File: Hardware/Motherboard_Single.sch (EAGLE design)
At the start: 63 parts, among them J1 MICROMOD-2222-C, J10 MICRO-SD-PUSH-PUSH-EXT-PIN, J2 Vertical Qwiic Connector, J4 QWIIC_RIGHT_ANGLE, J5 CORTEX_JTAG_DEBUG_MINIMUM_PTH, J6 MICROMOD_CARRIER, U2 MCP73831, U5 AP7361C-33

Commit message: Adds another standoff for qwiic boards around the lower left edge, adds silk
* Removes jumper for "VIN/VUSB"
* Correctly routes USB_VIN on processor connector to VIN
* Double routes PWR_EN for ESP32 Processor boards
* Moves SD Card up 0.04"
* Adds more measures
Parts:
- removed JP1: JUMPER-SMT_2_NC_TRACE_SILK, SparkFun-Jumpers:JUMPER-SMT_2_NC_TRACE_SILK
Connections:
- removed net USB_VIN: J1.USB_VIN
- removed net V_USB: BYP.2, F2.2, JP1.1, TP4.1
- net PWR_EN0: now also J1.AUD_LRCLK
- net VIN: now also BYP.2, F2.2, J1.USB_VIN, TP4.1; no longer JP1.2
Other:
- note added: "Buttons"
- note added: "v10"
- note removed: "Buttons and Switch"
- note removed: "v01"
- moved on the sheet: J13, S1, S2

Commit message: Adds 2 pin dip switch for charge selection, adds PCHAN MOSFET to VBATT net
* Adds better silk
* Moves stuff around schematic for better clarity
* Adds charge table to schematic
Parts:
- removed D7: 3A/10V/280mV, SparkFun-DiscreteSemi:DIODE-SCHOTTKY-BAT60A
- removed R6: 2.0k, SparkFun-Resistors:2.0KOHM-0603-1/10W-5%
- added Q1: 20V/4.2A/52mΩ/1.4W, SparkFun-DiscreteSemi:MOSFET_PCH-DMG2305UX-7
- added R3: 2.0k, SparkFun-Resistors:2.0KOHM-0603-1/10W-5%
- added R4: 10k, SparkFun-Resistors:10KOHM-0603-1/10W-1%
- added S3: DIP-02-SMD-50MIL, SparkFun-Switches:DIP-02-SMD-50MIL
- LOGO3: value OSHW-LOGOMINI -> OSHW-LOGOL; device SparkFun-Aesthetics:OSHW-LOGOMINI -> SparkFun-Aesthetics:OSHW-LOGOL
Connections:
- new net N$11: R4.2, S3.P$2
- new net N$7: R3.2, S3.P$1
- net GND: now also R3.1, R4.1; no longer R6.1
- net N$8: now also S3.P$3, S3.P$4; no longer R6.2
- net VCC: now also Q1.S; no longer D7.C
- net VIN: now also Q1.G
- net V_BATT: now also Q1.D; no longer D7.A
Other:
- note added: "1"
- note added: "1+2"
- note added: "100mA"
- note added: "166mA"
- note added: "2"
- note added: "500mA"
- note added: "Charge Current Selection"
- note added: "Standoff"
- note added: "Standoffs"
- note removed: "Charge current: 500mA (1000V/Rprog)"
- moved on the sheet: C3, C4, D4, D5, J13, J2, J4, J8, R5, S1, S2, TP1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

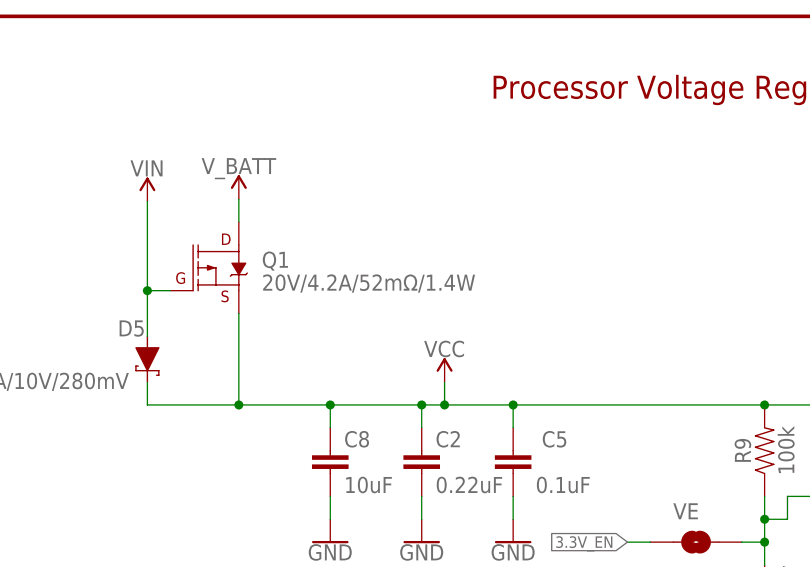
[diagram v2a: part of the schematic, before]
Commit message: Replaces MOSFET with another one
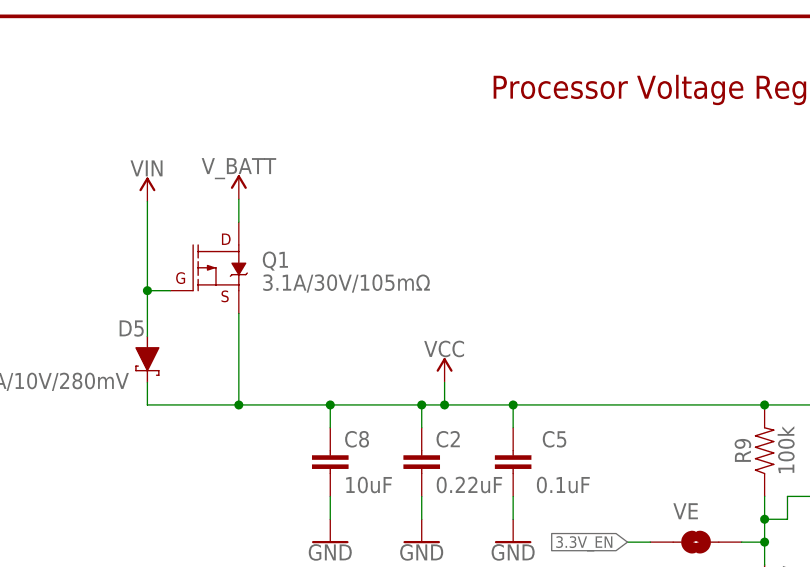
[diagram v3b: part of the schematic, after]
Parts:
- Q1: value 20V/4.2A/52mΩ/1.4W -> 3.1A/30V/105mΩ; device SparkFun-DiscreteSemi:MOSFET_PCH-DMG2305UX-7 -> SparkFun-DiscreteSemi:MOSFET_PCH-DMG2307L
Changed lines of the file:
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@@
 <part name="R4" library="SparkFun-Resistors" deviceset="10KOHM" device="-0603-1/10W-1%" value="10k"/>
 <part name="GND3" library="SparkFun-PowerSymbols" deviceset="GND" device=""/>
-<part name="Q1" library="SparkFun-DiscreteSemi" deviceset="MOSFET_PCH" device="-DMG2305UX-7" value="20V/4.2A/52mΩ/1.4W"/>
+<part name="Q1" library="SparkFun-DiscreteSemi" deviceset="MOSFET_PCH" device="-DMG2307L" value="3.1A/30V/105mΩ"/>
 <part name="GND5" library="SparkFun-PowerSymbols" deviceset="GND" device=""/>
 </parts>

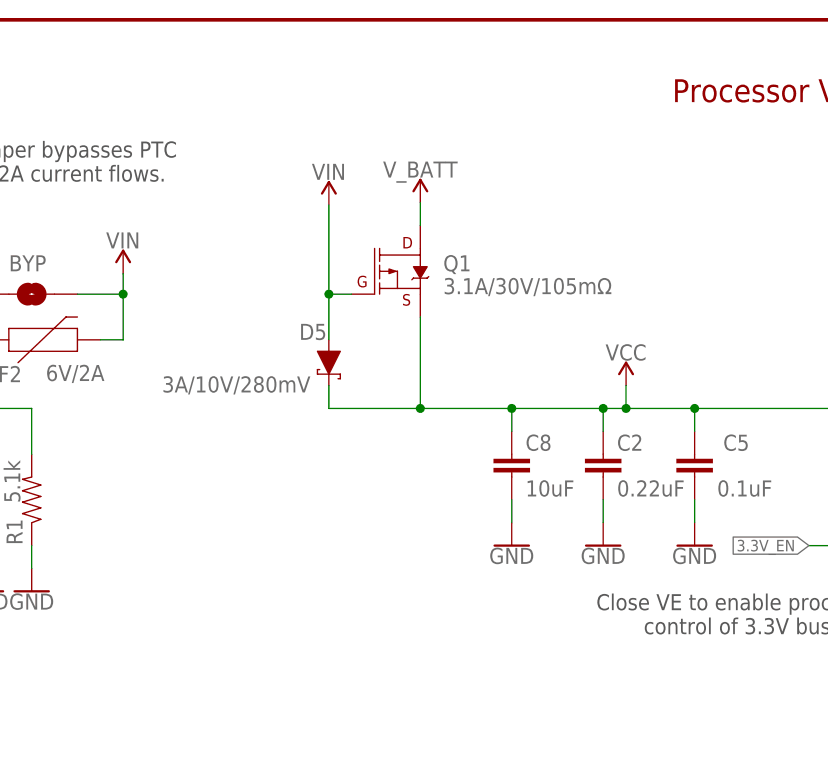
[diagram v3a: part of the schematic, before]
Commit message: Adds 10k pulldown to gate on PCHAN MOSFET, fixes length measurement
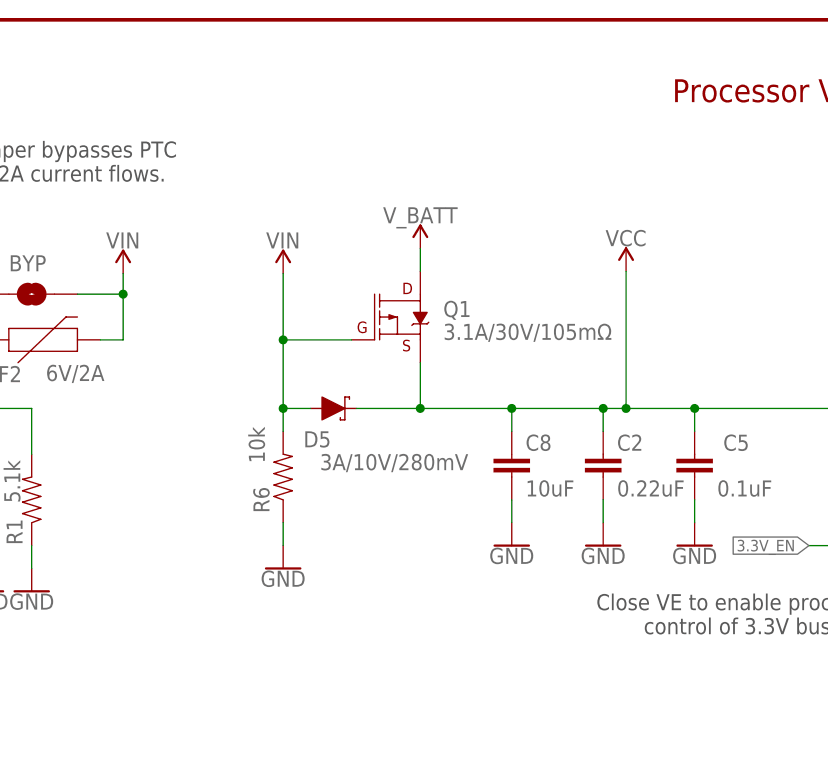
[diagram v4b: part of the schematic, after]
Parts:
- added R6: 10k, SparkFun-Resistors:10KOHM-0603-1/10W-1%
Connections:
- net GND: now also R6.1
- net VIN: now also R6.2
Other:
- moved on the sheet: D5, Q1
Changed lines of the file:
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@@
 <part name="Q1" library="SparkFun-DiscreteSemi" deviceset="MOSFET_PCH" device="-DMG2307L" value="3.1A/30V/105mΩ"/>
 <part name="GND5" library="SparkFun-PowerSymbols" deviceset="GND" device=""/>
+<part name="R6" library="SparkFun-Resistors" deviceset="10KOHM" device="-0603-1/10W-1%" value="10k"/>
+<part name="GND6" library="SparkFun-PowerSymbols" deviceset="GND" device=""/>
 </parts>
 <sheets>
@@
 <attribute name="VALUE" x="238.76" y="215.646" size="1.778" layer="96" rot="MR0" align="top-center"/>
 </instance>
-<instance part="SUPPLY27" gate="G$1" x="281.94" y="259.08" smashed="yes">
-<attribute name="VALUE" x="281.94" y="261.874" size="1.778" layer="96" align="bottom-center"/>
+<instance part="SUPPLY27" gate="G$1" x="281.94" y="254" smashed="yes">
+<attribute name="VALUE" x="281.94" y="256.794" size="1.778" layer="96" align="bottom-center"/>
 </instance>
 <instance part="U5" gate="G$1" x="360.68" y="231.14" smashed="yes">
@@
 <attribute name="VALUE" x="293.624" y="226.441" size="1.778" layer="96" font="vector"/>
 </instance>
-<instance part="SUPPLY28" gate="G$1" x="304.8" y="238.76" smashed="yes">
-<attribute name="VALUE" x="304.8" y="241.554" size="1.778" layer="96" align="bottom-center"/>
-</instance>
-<instance part="D5" gate="G$1" x="271.78" y="241.3" smashed="yes" rot="R270">
-<attribute name="NAME" x="268.478" y="243.84" size="1.778" layer="95" font="vector"/>
-<attribute name="VALUE" x="253.238" y="239.776" size="1.778" layer="96" font="vector" align="top-left"/>
+<instance part="SUPPLY28" gate="G$1" x="304.8" y="251.46" smashed="yes">
+<attribute name="VALUE" x="304.8" y="254.254" size="1.778" layer="96" align="bottom-center"/>
+</instance>
+<instance part="D5" gate="G$1" x="272.288" y="236.22" smashed="yes">
+<attribute name="NAME" x="272.034" y="233.68" size="1.778" layer="95" font="vector" rot="R180"/>
+<attribute name="VALUE" x="287.274" y="229.362" size="1.778" layer="96" font="vector" rot="R180" align="top-left"/>
 </instance>
 <instance part="5V_LED" gate="G$1" x="378.714" y="61.722" smashed="yes" rot="R90">
@@
 <attribute name="VALUE" x="378.714" y="51.308" size="1.778" layer="96" align="top-center"/>
 </instance>
-<instance part="SUPPLY13" gate="G$1" x="271.78" y="258.826" smashed="yes">
-<attribute name="VALUE" x="271.78" y="261.62" size="1.778" layer="96" align="bottom-center"/>
+<instance part="SUPPLY13" gate="G$1" x="266.7" y="251.206" smashed="yes">
+<attribute name="VALUE" x="266.7" y="254" size="1.778" layer="96" align="bottom-center"/>
 </instance>
 <instance part="SUPPLY24" gate="G$1" x="378.714" y="92.456" smashed="yes">
@@
 <attribute name="VALUE" x="276.86" y="131.826" size="1.778" layer="96" font="vector" rot="MR0" align="top-center"/>
 </instance>
-<instance part="Q1" gate="G$1" x="279.4" y="251.46" smashed="yes">
-<attribute name="NAME" x="284.48" y="251.46" size="1.778" layer="95" font="vector"/>
-<attribute name="VALUE" x="284.48" y="248.92" size="1.778" layer="96" font="vector"/>
+<instance part="Q1" gate="G$1" x="279.4" y="246.38" smashed="yes">
+<attribute name="NAME" x="284.48" y="246.38" size="1.778" layer="95" font="vector"/>
+<attribute name="VALUE" x="284.48" y="243.84" size="1.778" layer="96" font="vector"/>
 </instance>
 <instance part="GND5" gate="1" x="193.04" y="5.08" smashed="yes">
 <attribute name="VALUE" x="193.04" y="4.826" size="1.778" layer="96" font="vector" align="top-center"/>
+</instance>
+<instance part="R6" gate="G$1" x="266.7" y="228.6" smashed="yes" rot="R90">
+<attribute name="NAME" x="265.176" y="226.06" size="1.778" layer="95" font="vector" rot="R90" align="bottom-center"/>
+<attribute name="VALUE" x="262.89" y="232.156" size="1.778" layer="96" font="vector" rot="R90" align="top-center"/>
+</instance>
+<instance part="GND6" gate="1" x="266.7" y="218.44" smashed="yes">
+<attribute name="VALUE" x="266.7" y="218.186" size="1.778" layer="96" align="top-center"/>
 </instance>
 </instances>
@@
 <wire x1="192.024" y1="164.338" x2="192.024" y2="166.878" width="0.1524" layer="91"/>
 </segment>
+<segment>
+<pinref part="R6" gate="G$1" pin="1"/>
+<wire x1="266.7" y1="223.52" x2="266.7" y2="220.98" width="0.1524" layer="91"/>
+<pinref part="GND6" gate="1" pin="GND"/>
+</segment>
 </net>
 <net name="PWR_EN0" class="0">
@@
 <pinref part="D5" gate="G$1" pin="A"/>
 <pinref part="SUPPLY13" gate="G$1" pin="VIN"/>
-<wire x1="271.78" y1="243.84" x2="271.78" y2="248.92" width="0.1524" layer="91"/>
 <pinref part="Q1" gate="G$1" pin="G"/>
-<wire x1="271.78" y1="248.92" x2="271.78" y2="258.826" width="0.1524" layer="91"/>
-<wire x1="274.32" y1="248.92" x2="271.78" y2="248.92" width="0.1524" layer="91"/>
-<junction x="271.78" y="248.92"/>
+<wire x1="274.32" y1="243.84" x2="266.7" y2="243.84" width="0.1524" layer="91"/>
+<wire x1="266.7" y1="243.84" x2="266.7" y2="251.206" width="0.1524" layer="91"/>
+<pinref part="R6" gate="G$1" pin="2"/>
+<wire x1="266.7" y1="233.68" x2="266.7" y2="236.22" width="0.1524" layer="91"/>
+<junction x="266.7" y="243.84"/>
+<wire x1="266.7" y1="236.22" x2="266.7" y2="243.84" width="0.1524" layer="91"/>
+<wire x1="269.748" y1="236.22" x2="266.7" y2="236.22" width="0.1524" layer="91"/>
+<junction x="266.7" y="236.22"/>
 </segment>
 <segment>
@@
 <pinref part="Q1" gate="G$1" pin="D"/>
 <pinref part="SUPPLY27" gate="G$1" pin="V_BATT"/>
-<wire x1="281.94" y1="259.08" x2="281.94" y2="256.54" width="0.1524" layer="91"/>
+<wire x1="281.94" y1="254" x2="281.94" y2="251.46" width="0.1524" layer="91"/>
 </segment>
 </net>
@@
 <pinref part="C8" gate="G$1" pin="1"/>
 <pinref part="SUPPLY28" gate="G$1" pin="VCC"/>
-<wire x1="304.8" y1="236.22" x2="304.8" y2="238.76" width="0.1524" layer="91"/>
+<wire x1="304.8" y1="236.22" x2="304.8" y2="251.46" width="0.1524" layer="91"/>
 <junction x="304.8" y="236.22"/>
 <wire x1="292.1" y1="236.22" x2="281.94" y2="236.22" width="0.1524" layer="91"/>
 <junction x="292.1" y="236.22"/>
 <pinref part="D5" gate="G$1" pin="C"/>
-<wire x1="281.94" y1="236.22" x2="271.78" y2="236.22" width="0.1524" layer="91"/>
-<wire x1="271.78" y1="236.22" x2="271.78" y2="238.76" width="0.1524" layer="91"/>
+<wire x1="281.94" y1="236.22" x2="274.828" y2="236.22" width="0.1524" layer="91"/>
 <pinref part="Q1" gate="G$1" pin="S"/>
-<wire x1="281.94" y1="246.38" x2="281.94" y2="236.22" width="0.1524" layer="91"/>
+<wire x1="281.94" y1="241.3" x2="281.94" y2="236.22" width="0.1524" layer="91"/>
 <junction x="281.94" y="236.22"/>
 </segment>

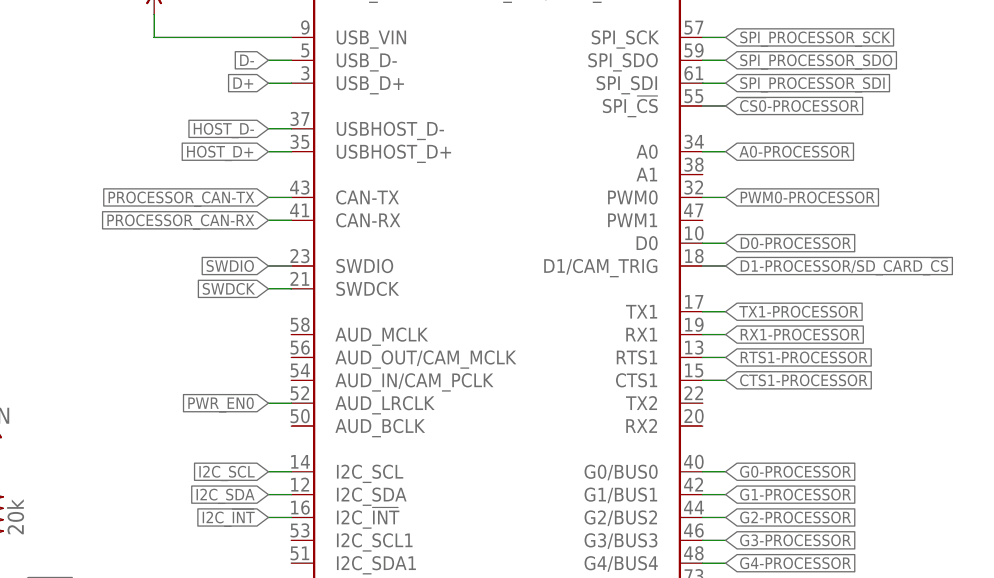
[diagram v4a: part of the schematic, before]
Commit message: Adds prod_id to function board connector, double routes power enable to A1 and previous pin
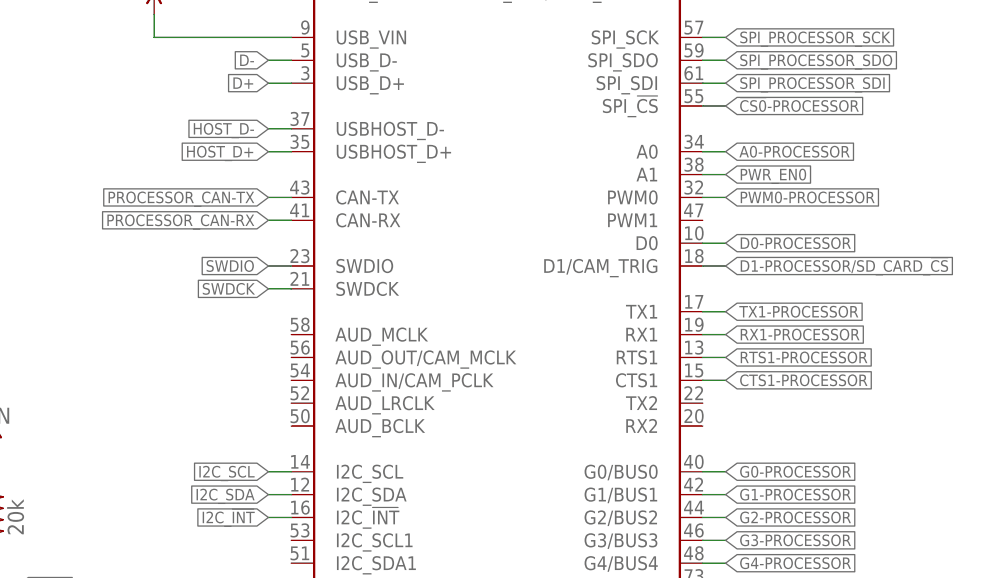
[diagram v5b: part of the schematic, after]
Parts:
- H3, H4, H8: value STAND-OFF-REFLOW2.5MM_TALL -> STAND-OFF-REFLOW-M2.5_2.5MM_TALL; device SparkFun-Hardware:STAND-OFF-REFLOW2.5MM_TALL -> SparkFun-Hardware:STAND-OFF-REFLOW-M2.5_2.5MM_TALL
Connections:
- net PWR_EN0: now also J1.A1; no longer J1.AUD_LRCLK
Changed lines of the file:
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@@
 <part name="J4" library="SparkFun-Connectors" deviceset="QWIIC_CONNECTOR" device="JS-1MM" value="QWIIC_RIGHT_ANGLE"/>
 <part name="FRAME1" library="SparkFun-Aesthetics" deviceset="FRAME-LEDGER" device=""/>
-<part name="H3" library="SparkFun-Hardware" deviceset="STAND-OFF-REFLOW" device="2.5MM_TALL"/>
-<part name="H8" library="SparkFun-Hardware" deviceset="STAND-OFF-REFLOW" device="2.5MM_TALL"/>
+<part name="H3" library="SparkFun-Hardware" deviceset="STAND-OFF-REFLOW" device="-M2.5_2.5MM_TALL"/>
+<part name="H8" library="SparkFun-Hardware" deviceset="STAND-OFF-REFLOW" device="-M2.5_2.5MM_TALL"/>
 <part name="H14" library="SparkFun-Hardware" deviceset="STAND-OFF" device="TIGHT"/>
 <part name="H15" library="SparkFun-Hardware" deviceset="STAND-OFF" device="TIGHT"/>
@@
 <part name="C12" library="SparkFun-Capacitors" deviceset="0.1UF" device="-0603-25V-(+80/-20%)" value="0.1uF"/>
 <part name="GND36" library="SparkFun-PowerSymbols" deviceset="GND" device=""/>
-<part name="H4" library="SparkFun-Hardware" deviceset="STAND-OFF-REFLOW" device="2.5MM_TALL"/>
+<part name="H4" library="SparkFun-Hardware" deviceset="STAND-OFF-REFLOW" device="-M2.5_2.5MM_TALL"/>
 <part name="GND40" library="SparkFun-PowerSymbols" deviceset="GND" device=""/>
 <part name="SUPPLY9" library="SparkFun-PowerSymbols" deviceset="VIN" device=""/>
@@
 </segment>
 <segment>
-<wire x1="73.66" y1="66.04" x2="71.12" y2="66.04" width="0.1524" layer="91"/>
-<label x="71.12" y="66.04" size="1.27" layer="95" font="vector" rot="R180" xref="yes"/>
-<pinref part="J1" gate="J1" pin="AUD_LRCLK"/>
+<pinref part="J1" gate="J1" pin="A1"/>
+<wire x1="121.92" y1="91.44" x2="119.38" y2="91.44" width="0.1524" layer="91"/>
+<label x="121.92" y="91.44" size="1.27" layer="95" font="vector" xref="yes"/>
 </segment>
 </net>
